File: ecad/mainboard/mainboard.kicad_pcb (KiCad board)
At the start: 2 copper layers, 31 parts, among them J1 Dot Matrix Side A (M), J2 Dot Matrix Side A (F), J3 Dot Matrix Side B (F), J4 Dot Matrix Side B (M), J5 ESP32C3 Super Mini Left, J6 ESP32C3 Super Mini Right, J7 IO Expander Module - Left, J8 IO Expander Module - Right, SW1 Left Button, SW2 Right Button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

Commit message: place io expander (pcf8575)
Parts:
- moved U1 30.7 mm to (112.5, 78.7), turned to -90 degrees
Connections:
- R10 pad 2: /P11 -> /P16
- R11 pad 2: /P12 -> /P15
- R12 pad 2: /P13 -> /P14
- R13 pad 2: /P14 -> /P13
- R14 pad 2: /P15 -> /P12
- R15 pad 2: /P16 -> /P11
- R16 pad 2: /P17 -> /P10
- R9 pad 2: /P10 -> /P17
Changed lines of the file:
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@@
 			(layers "F.Cu" "F.Mask" "F.Paste")
 			(roundrect_rratio 0.243902)
-			(net "/P13")
+			(net "/P14")
 			(pintype "passive")
 		)
@@
 			(layers "F.Cu" "F.Mask" "F.Paste")
 			(roundrect_rratio 0.243902)
-			(net "/P17")
+			(net "/P10")
 			(pintype "passive")
 		)
@@
 			(layers "F.Cu" "F.Mask" "F.Paste")
 			(roundrect_rratio 0.243902)
-			(net "/P15")
+			(net "/P12")
 			(pintype "passive")
 		)
@@
 			(layers "F.Cu" "F.Mask" "F.Paste")
 			(roundrect_rratio 0.243902)
-			(net "/P10")
+			(net "/P17")
 			(pintype "passive")
 		)
@@
 			(layers "F.Cu" "F.Mask" "F.Paste")
 			(roundrect_rratio 0.243902)
-			(net "/P11")
+			(net "/P16")
 			(pintype "passive")
 		)
@@
 			(layers "F.Cu" "F.Mask" "F.Paste")
 			(roundrect_rratio 0.243902)
-			(net "/P16")
+			(net "/P11")
 			(pintype "passive")
 		)
@@
 			(layers "F.Cu" "F.Mask" "F.Paste")
 			(roundrect_rratio 0.243902)
-			(net "/P14")
+			(net "/P13")
 			(pintype "passive")
 		)
@@
 			(layers "F.Cu" "F.Mask" "F.Paste")
 			(roundrect_rratio 0.243902)
-			(net "/P12")
+			(net "/P15")
 			(pintype "passive")
 		)
@@
 	(footprint "Package_SO:SSOP-24_5.3x8.2mm_P0.65mm"
 		(layer "F.Cu")
-		(at 142.8175 83.42 90)
+		(at 112.481 78.74 -90)
 		(descr "SSOP, 24 Pin (JEDEC MO-150 variation AG, 1.75mm body thickness, https://www.jedec.org/document_search?search_api_views_fulltext=MO-150, https://ww1.microchip.com/downloads/en/PackagingSpec/00000049BQ.pdf#page=398, https://www.analog.com/media/en/package-pcb-resources/package/pkg_pdf/ltc-legacy-ssop/ssop_24_05-08-1640.pdf)")
 		(tags "SSOP SO")
 		(property "Reference" "U1"
-			(at 0 -5.05 90)
+			(at 0 -5.629 180)
 			(layer "F.SilkS")
 			(effects
@@
 		(duplicate_pad_numbers_are_jumpers no)
 		(fp_line
-			(start 2.76 -4.21)
-			(end 2.76 -4.035)
+			(start -2.76 4.21)
+			(end -2.76 4.035)
 			(stroke
 				(width 0.12)
@@
 		)
 		(fp_line
-			(start -2.76 -4.21)
-			(end 2.76 -4.21)
+			(start 2.76 4.21)
+			(end -2.76 4.21)
 			(stroke
 				(width 0.12)
@@
 		)
 		(fp_line
-			(start -2.76 -4.035)
-			(end -2.76 -4.21)
+			(start 2.76 4.035)
+			(end 2.76 4.21)
 			(stroke
 				(width 0.12)
@@
 		)
 		(fp_line
-			(start 2.76 4.035)
-			(end 2.76 4.21)
+			(start -2.76 -4.035)
+			(end -2.76 -4.21)
 			(stroke
 				(width 0.12)
@@
 		)
 		(fp_line
-			(start 2.76 4.21)
-			(end -2.76 4.21)
+			(start -2.76 -4.21)
+			(end 2.76 -4.21)
 			(stroke
 				(width 0.12)
@@
 		)
 		(fp_line
-			(start -2.76 4.21)
-			(end -2.76 4.035)
+			(start 2.76 -4.21)
+			(end 2.76 -4.035)
 			(stroke
 				(width 0.12)
@@
 		)
 		(fp_line
-			(start 2.9 -4.35)
-			(end 2.9 -4.03)
+			(start -2.9 4.35)
+			(end -2.9 4.03)
 			(stroke
 				(width 0.05)
@@
 		)
 		(fp_line
-			(start -2.9 -4.35)
-			(end 2.9 -4.35)
+			(start 2.9 4.35)
+			(end -2.9 4.35)
 			(stroke
 				(width 0.05)
@@
 		)
 		(fp_line
-			(start 4.7 -4.03)
-			(end 4.7 4.03)
+			(start -4.7 4.03)
+			(end -4.7 -4.03)
 			(stroke
 				(width 0.05)
@@
 		)
 		(fp_line
-			(start 2.9 -4.03)
-			(end 4.7 -4.03)
+			(start -2.9 4.03)
+			(end -4.7 4.03)
 			(stroke
 				(width 0.05)
@@
 		)
 		(fp_line
-			(start -2.9 -4.03)
-			(end -2.9 -4.35)
+			(start 2.9 4.03)
+			(end 2.9 4.35)
 			(stroke
 				(width 0.05)
@@
 		)
 		(fp_line
-			(start -4.7 -4.03)
-			(end -2.9 -4.03)
+			(start 4.7 4.03)
+			(end 2.9 4.03)
 			(stroke
 				(width 0.05)
@@
 		)
 		(fp_line
-			(start 4.7 4.03)
-			(end 2.9 4.03)
+			(start -4.7 -4.03)
+			(end -2.9 -4.03)
 			(stroke
 				(width 0.05)
@@
 		)
 		(fp_line
-			(start 2.9 4.03)
-			(end 2.9 4.35)
+			(start -2.9 -4.03)
+			(end -2.9 -4.35)
 			(stroke
 				(width 0.05)
@@
 		)
 		(fp_line
-			(start -2.9 4.03)
-			(end -4.7 4.03)
+			(start 2.9 -4.03)
+			(end 4.7 -4.03)
 			(stroke
 				(width 0.05)
@@
 		)
 		(fp_line
-			(start -4.7 4.03)
-			(end -4.7 -4.03)
+			(start 4.7 -4.03)
+			(end 4.7 4.03)
 			(stroke
 				(width 0.05)
@@
 		)
 		(fp_line
-			(start 2.9 4.35)
-			(end -2.9 4.35)
+			(start -2.9 -4.35)
+			(end 2.9 -4.35)
 			(stroke
 				(width 0.05)
@@
 		)
 		(fp_line
-			(start -2.9 4.35)
-			(end -2.9 4.03)
+			(start 2.9 -4.35)
+			(end 2.9 -4.03)
 			(stroke
 				(width 0.05)
@@
 		)
 		(pad "1" smd roundrect
-			(at -3.5 -3.575 90)
+			(at -3.5 -3.575 270)
 			(size 1.9 0.4)
 			(layers "F.Cu" "F.Mask" "F.Paste")
@@
 		)
 		(pad "2" smd roundrect
-			(at -3.5 -2.925 90)
+			(at -3.5 -2.925 270)
 			(size 1.9 0.4)
 			(layers "F.Cu" "F.Mask" "F.Paste")
@@
 		)
 		(pad "3" smd roundrect
-			(at -3.5 -2.275 90)
+			(at -3.5 -2.275 270)
 			(size 1.9 0.4)
 			(layers "F.Cu" "F.Mask" "F.Paste")
@@
 		)
 		(pad "4" smd roundrect
-			(at -3.5 -1.625 90)
+			(at -3.5 -1.625 270)
 			(size 1.9 0.4)
 			(layers "F.Cu" "F.Mask" "F.Paste")
@@
 		)
 		(pad "5" smd roundrect
-			(at -3.5 -0.975 90)
+			(at -3.5 -0.975 270)
 			(size 1.9 0.4)
 			(layers "F.Cu" "F.Mask" "F.Paste")
@@
 		)
 		(pad "6" smd roundrect
-			(at -3.5 -0.325 90)
+			(at -3.5 -0.325 270)
 			(size 1.9 0.4)
 			(layers "F.Cu" "F.Mask" "F.Paste")
@@
 		)
 		(pad "7" smd roundrect
-			(at -3.5 0.325 90)
+			(at -3.5 0.325 270)
 			(size 1.9 0.4)
 			(layers "F.Cu" "F.Mask" "F.Paste")
@@
 		)
 		(pad "8" smd roundrect
-			(at -3.5 0.975 90)
+			(at -3.5 0.975 270)
 			(size 1.9 0.4)
 			(layers "F.Cu" "F.Mask" "F.Paste")
@@
 		)
 		(pad "9" smd roundrect
-			(at -3.5 1.625 90)
+			(at -3.5 1.625 270)
 			(size 1.9 0.4)
 			(layers "F.Cu" "F.Mask" "F.Paste")
@@
 		)
 		(pad "10" smd roundrect
-			(at -3.5 2.275 90)
+			(at -3.5 2.275 270)
 			(size 1.9 0.4)
 			(layers "F.Cu" "F.Mask" "F.Paste")
@@
 		)
 		(pad "11" smd roundrect
-			(at -3.5 2.925 90)
+			(at -3.5 2.925 270)
 			(size 1.9 0.4)
 			(layers "F.Cu" "F.Mask" "F.Paste")
@@
 		)
 		(pad "12" smd roundrect
-			(at -3.5 3.575 90)
+			(at -3.5 3.575 270)
 			(size 1.9 0.4)
 			(layers "F.Cu" "F.Mask" "F.Paste")
@@
 		)
 		(pad "13" smd roundrect
-			(at 3.5 3.575 90)
+			(at 3.5 3.575 270)
 			(size 1.9 0.4)
 			(layers "F.Cu" "F.Mask" "F.Paste")
@@
 		)
 		(pad "14" smd roundrect
-			(at 3.5 2.925 90)
+			(at 3.5 2.925 270)
 			(size 1.9 0.4)
 			(layers "F.Cu" "F.Mask" "F.Paste")
@@
 		)
 		(pad "15" smd roundrect
-			(at 3.5 2.275 90)
+			(at 3.5 2.275 270)
 			(size 1.9 0.4)
 			(layers "F.Cu" "F.Mask" "F.Paste")
@@
 		)
 		(pad "16" smd roundrect
-			(at 3.5 1.625 90)
+			(at 3.5 1.625 270)
 			(size 1.9 0.4)
 			(layers "F.Cu" "F.Mask" "F.Paste")
@@
 		)
 		(pad "17" smd roundrect
-			(at 3.5 0.975 90)
+			(at 3.5 0.975 270)
 			(size 1.9 0.4)
 			(layers "F.Cu" "F.Mask" "F.Paste")
@@
 		)
 		(pad "18" smd roundrect
-			(at 3.5 0.325 90)
+			(at 3.5 0.325 270)
 			(size 1.9 0.4)
 			(layers "F.Cu" "F.Mask" "F.Paste")
@@
 		)
 		(pad "19" smd roundrect
-			(at 3.5 -0.325 90)
+			(at 3.5 -0.325 270)
 			(size 1.9 0.4)
 			(layers "F.Cu" "F.Mask" "F.Paste")
@@
 		)
 		(pad "20" smd roundrect
-			(at 3.5 -0.975 90)
+			(at 3.5 -0.975 270)
 			(size 1.9 0.4)
 			(layers "F.Cu" "F.Mask" "F.Paste")
@@
 		)
 		(pad "21" smd roundrect
-			(at 3.5 -1.625 90)
+			(at 3.5 -1.625 270)
 			(size 1.9 0.4)
 			(layers "F.Cu" "F.Mask" "F.Paste")
@@
 		)
 		(pad "22" smd roundrect
-			(at 3.5 -2.275 90)
+			(at 3.5 -2.275 270)
 			(size 1.9 0.4)
 			(layers "F.Cu" "F.Mask" "F.Paste")
@@
 		)
 		(pad "23" smd roundrect
-			(at 3.5 -2.925 90)
+			(at 3.5 -2.925 270)
 			(size 1.9 0.4)
 			(layers "F.Cu" "F.Mask" "F.Paste")
@@
 		)
 		(pad "24" smd roundrect
-			(at 3.5 -3.575 90)
+			(at 3.5 -3.575 270)
 			(size 1.9 0.4)
 			(layers "F.Cu" "F.Mask" "F.Paste")

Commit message: remove extra pin headers for the dot matrix
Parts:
- removed the J1 at (120.6, 60.3)
- removed the J4 at (120.6, 97.2)
- J5: renamed from J2; value Dot Matrix Side A (F) -> Dot Matrix Side A
- J6: renamed from J3; value Dot Matrix Side B (F) -> Dot Matrix Side B
- renumbered J5 to J1, J6 to J2, J7 to J3, J8 to J4

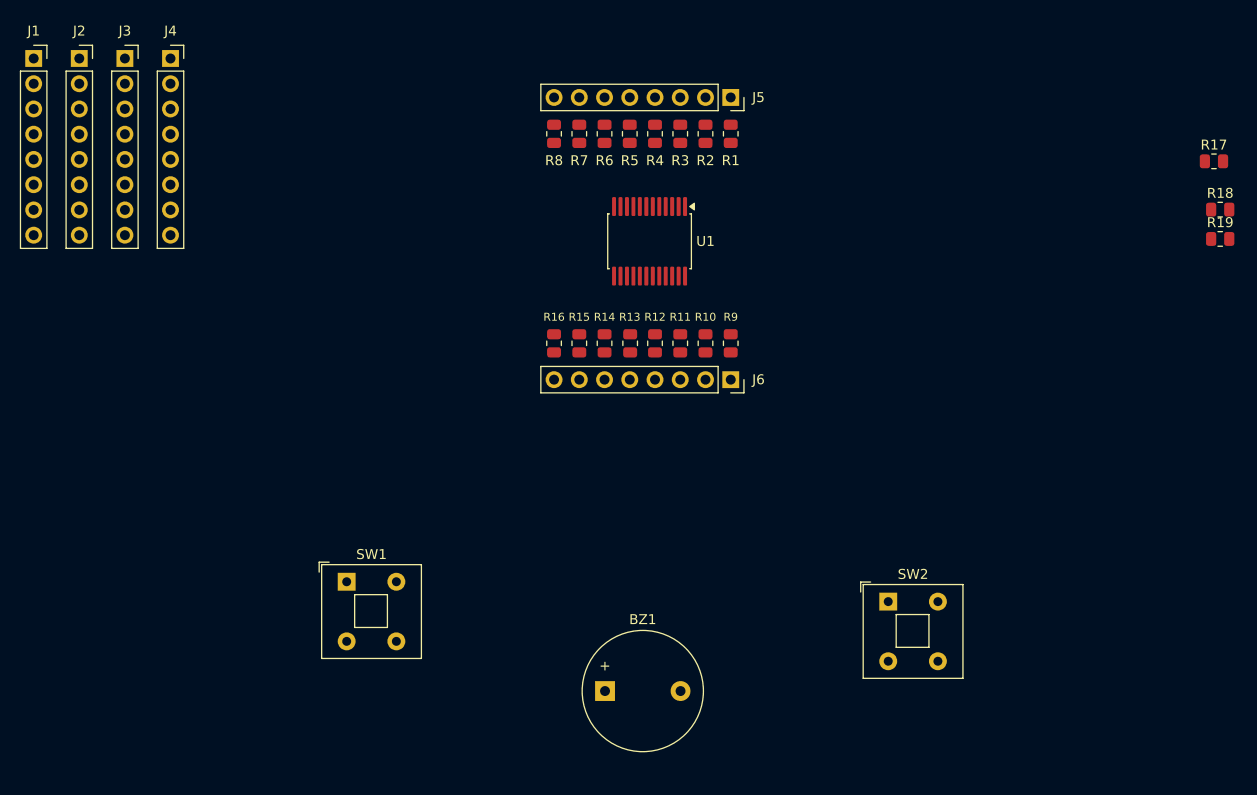
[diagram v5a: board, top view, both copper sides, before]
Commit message: remove headers for io expander module and route tracks for the dot matrix
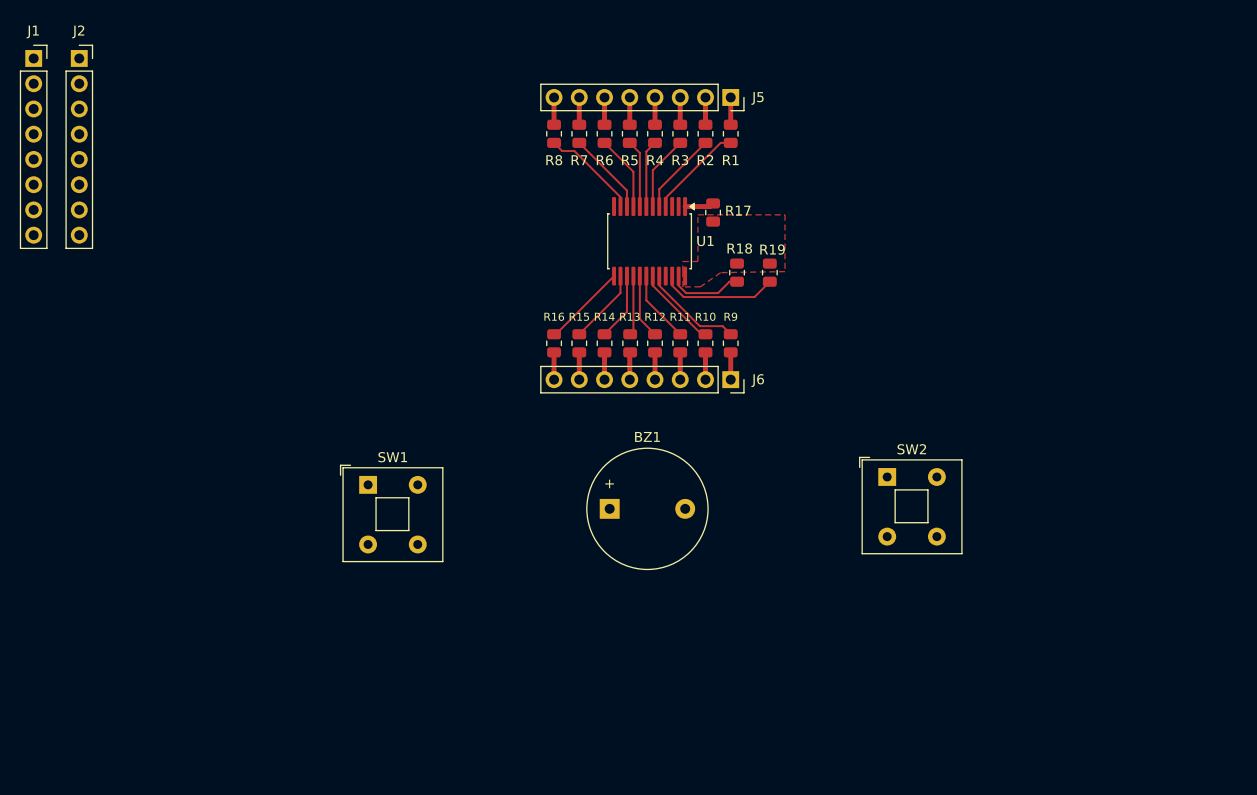
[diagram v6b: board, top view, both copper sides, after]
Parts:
- removed J3: IO Expander Module - Left, Connector_PinSocket_2.54mm:PinSocket_1x08_P2.54mm_Vertical
- removed J4: IO Expander Module - Right, Connector_PinSocket_2.54mm:PinSocket_1x08_P2.54mm_Vertical
- moved R17 50.7 mm to (118.9, 75.8), turned to 90 degrees
- moved R18 49.0 mm to (121.3, 81.9), turned to -90 degrees
- moved R19 45.4 mm to (124.6, 81.9), turned to -90 degrees
- moved BZ1 18.3 mm to (108.5, 105.7)
- moved SW2 12.5 mm to (136.4, 102.5)
- moved SW1 9.99 mm to (84.2, 103.2)
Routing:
- net /SCL: track 0.00 -> 11.9 mm
- net /P17: track 0.00 -> 10.2 mm
- net /P7: track 0.00 -> 9.90 mm
- net /P0: track 0.00 -> 9.71 mm
- net /P10: track 0.00 -> 8.46 mm
- net /P6: track 0.00 -> 8.39 mm
- net /P1: track 0.00 -> 8.33 mm
- net /P16: track 0.00 -> 8.28 mm
- net /SDA: track 0.00 -> 7.62 mm
- net /P5: track 0.00 -> 7.61 mm
- net /P11: track 0.00 -> 7.57 mm
- net /P2: track 0.00 -> 7.55 mm
- net /P15: track 0.00 -> 7.27 mm
- net /P4: track 0.00 -> 6.83 mm
- net /P12: track 0.00 -> 6.79 mm
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- added copper zone on F.Cu, net +3.3V

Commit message: add edge cuts to board
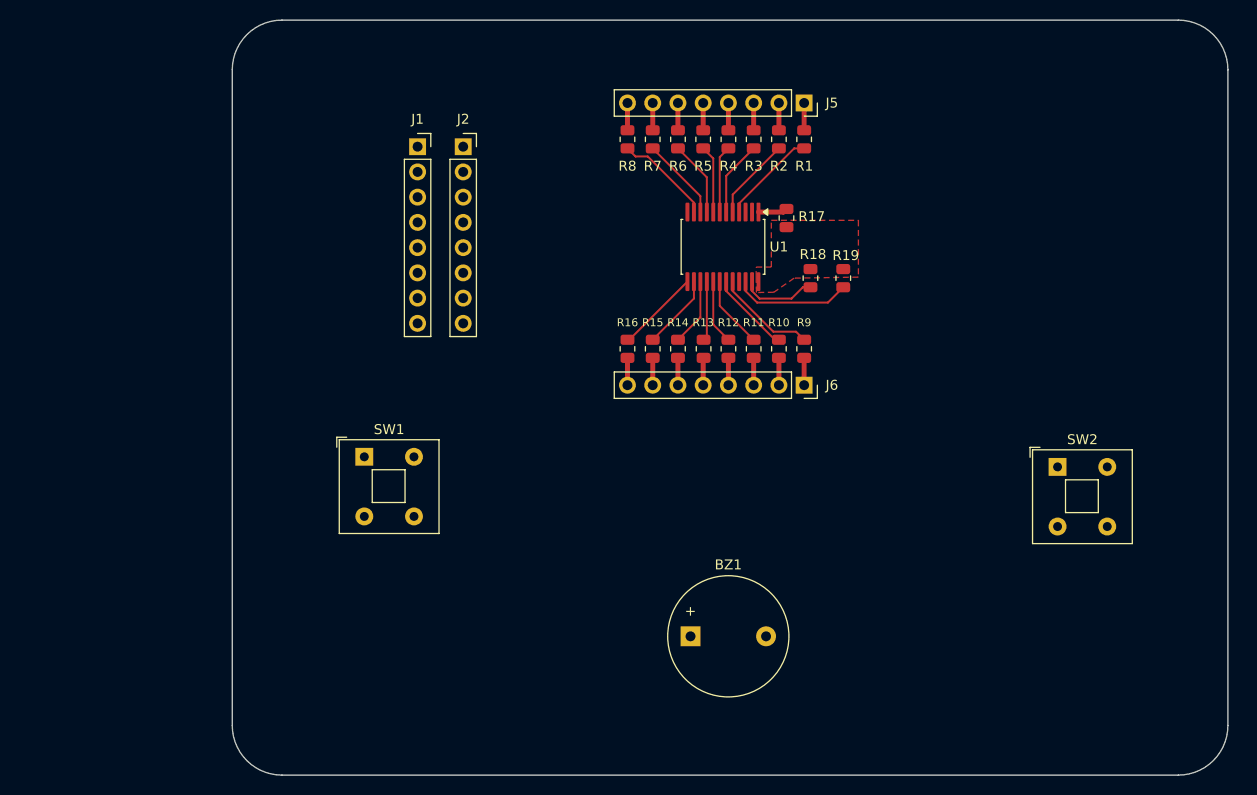
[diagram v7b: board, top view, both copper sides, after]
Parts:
- moved J1 39.6 mm to (89.1, 69.2)
- moved J2 39.6 mm to (93.7, 69.2)
- moved SW2 17.2 mm to (153.5, 101.4)
- moved BZ1 15.2 mm to (116.6, 118.5)
- moved R1 7.41 mm to (128.0, 68.5)
- moved R18 7.41 mm to (128.7, 82.4)
- moved R3 7.41 mm to (123.0, 68.5)
- moved R5 7.41 mm to (117.9, 68.5)
- moved R7 7.41 mm to (112.8, 68.5)
- moved U1 7.41 mm to (119.9, 79.3)
- moved J5 7.41 mm to (128.0, 64.8)
- moved J6 7.41 mm to (128.0, 93.2)
- moved R11 7.41 mm to (123.0, 89.6)
- moved R15 7.41 mm to (112.8, 89.6)
- moved R9 7.41 mm to (128.0, 89.6)
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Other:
- board outline added: 100.2 x 76 mm

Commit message: place switches and buzzer
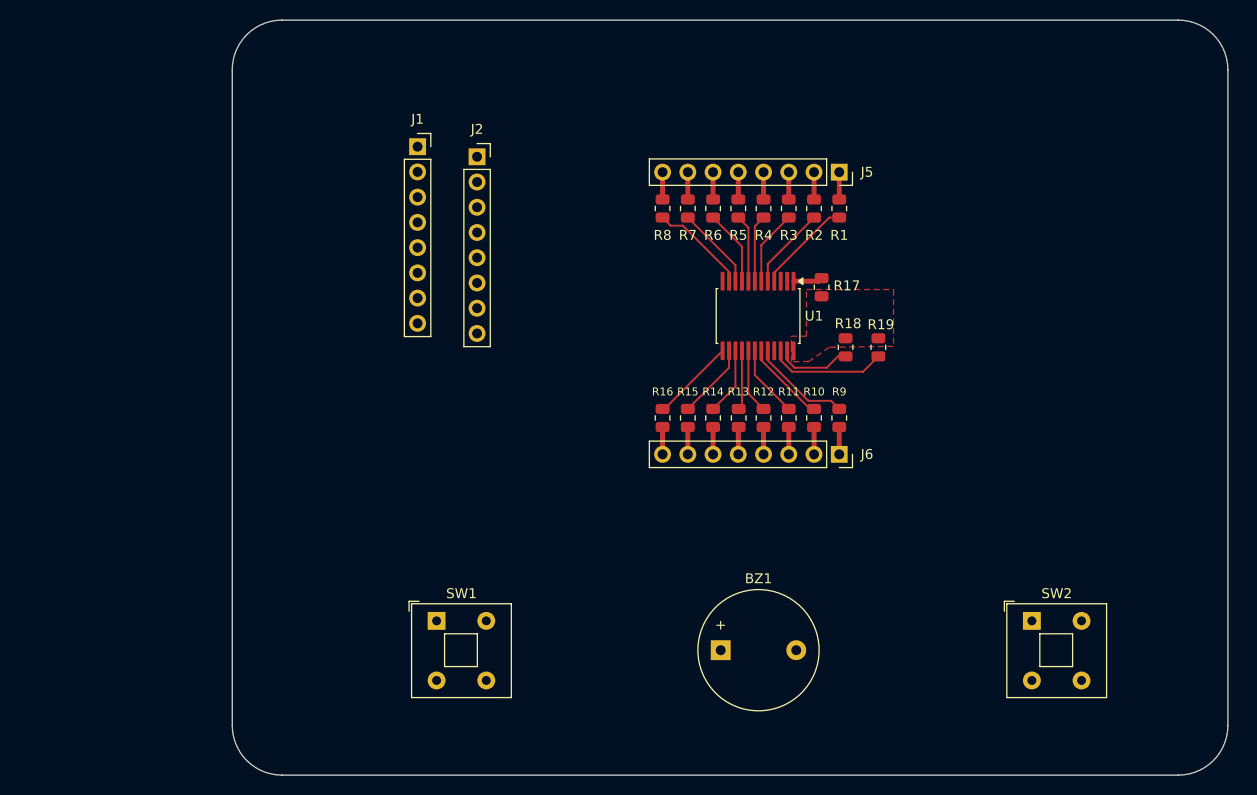
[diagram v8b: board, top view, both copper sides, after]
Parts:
- moved SW1 18.0 mm to (91.0, 116.9)
- moved SW2 15.7 mm to (151.0, 116.9)
- moved R10 7.81 mm to (129.0, 96.5)
- moved R17 7.81 mm to (129.8, 83.4)
- moved R2 7.81 mm to (129.0, 75.4)
- moved R11 7.81 mm to (126.5, 96.5)
- moved R12 7.81 mm to (124.0, 96.5)
- moved R13 7.81 mm to (121.5, 96.5)
- moved R14 7.81 mm to (118.9, 96.5)
- moved R16 7.81 mm to (113.8, 96.5)
- moved R3 7.81 mm to (126.5, 75.4)
- moved R4 7.81 mm to (124.0, 75.4)
- moved R5 7.81 mm to (121.4, 75.4)
- moved R6 7.81 mm to (118.9, 75.4)
- moved R8 7.81 mm to (113.8, 75.4)
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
